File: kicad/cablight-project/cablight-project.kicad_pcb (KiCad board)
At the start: 4 copper layers, 70.1 x 40 mm, 55 parts, among them J3 Screw_Term_1x4_5mm, M2.5 MountingHole_2.7mm_M2.5_ISO73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, Q1 IRLB8721PBF, SW3 switch_SPDT_SLW_121586, T1 ISL85410, U3 ESP32-S3-WROOM-1U

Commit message: drc checks
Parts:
- moved R1 1.00 mm to (-52.5, 5.50)
- moved D2 0.40 mm to (-32.1, 2.50)
- moved M2.5 0.18 mm to (-24.6, 3.15)
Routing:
- net BTN: track 45.1 -> 46.7 mm
- net /VBUS: track 31.1 -> 30.5 mm
- net D-: track 14.4 -> 15.0 mm

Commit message: 99 percent layout v1
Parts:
- added M2.5: MountingHole_2.7mm_M2.5_ISO7380_Pad_TopOnly, MountingHole:MountingHole_2.7mm_M2.5_ISO7380_Pad_TopOnly, F.Cu at (-24.6, 29.4)
- C13: moved to B.Cu
- moved C13 8.41 mm to (-24.6, 25.9), turned to 180 degrees
- moved R2 5.47 mm to (-46.8, 28.6)
- moved BOOT1 5.04 mm to (-40.4, 25.4), turned to 180 degrees
- moved RESET1 4.72 mm to (-47.8, 25.4), turned to 180 degrees
- moved C6 3.26 mm to (-51.2, 22.6)
- moved R3 2.93 mm to (-51.1, 25.4)
- moved C7 1.37 mm to (-46.7, 26.1)
- moved RCWL-1601 0.60 mm to (-24.6, 17.1)
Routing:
- net 3.3V: track 61.7 -> 141.2 mm, vias 4 -> 6
- net Net-(D10-A): track 0.20 -> 5.41 mm
- net BTN: track 46.7 -> 44.3 mm
- net PG: track 44.6 -> 42.4 mm
- net Net-(T1-FB): track 7.24 -> 9.34 mm
- net GND: track 6.11 -> 7.49 mm, vias 12 -> 15
- net Net-(USBC-V1-CC2): track 7.35 -> 8.62 mm
- net Net-(U3-GPIO0/BOOT): track 42.4 -> 41.2 mm
- net 24VDC: track 15.0 -> 14.5 mm
- net ECHO: track 23.8 -> 24.4 mm
- net DIP3: track 24.4 -> 23.9 mm
- added copper zone on In2.Cu, net GND
- removed copper zone on In2.Cu, net 3.3V
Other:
- outline, holes or cut-outs redrawn
- board text added: "C11~"
- board text removed: "TURN THESE AROUND"

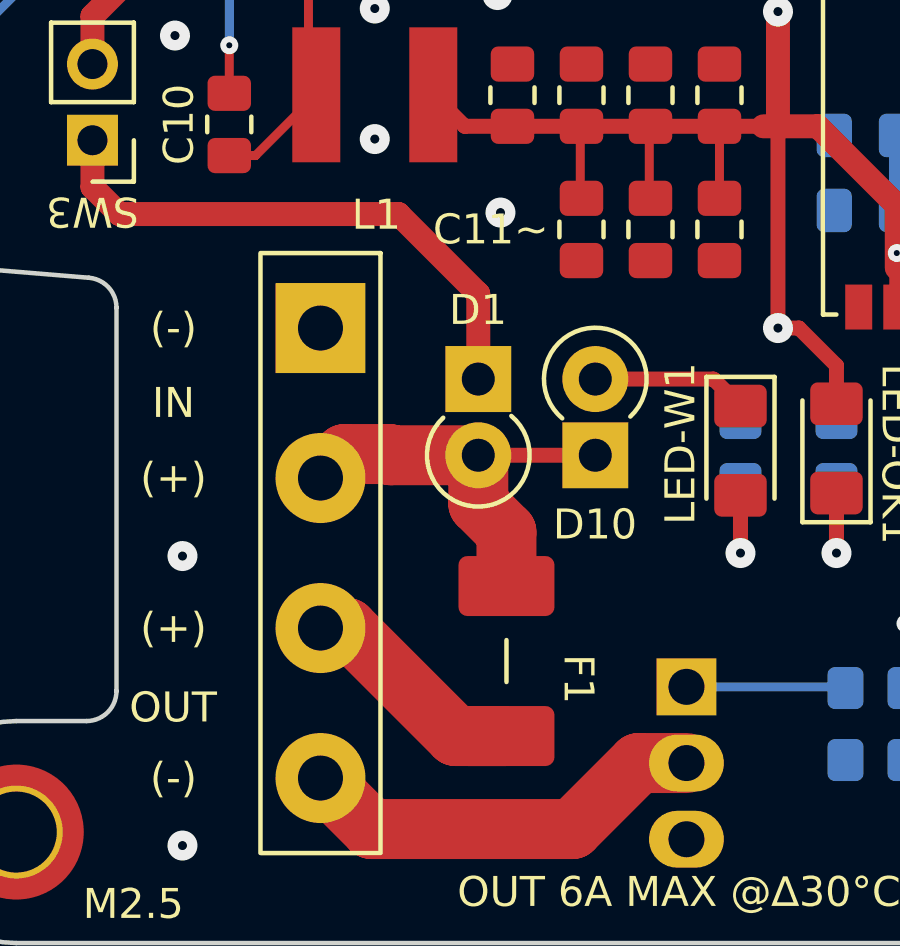
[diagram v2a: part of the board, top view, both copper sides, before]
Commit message: change fuse pkg & add datasheets
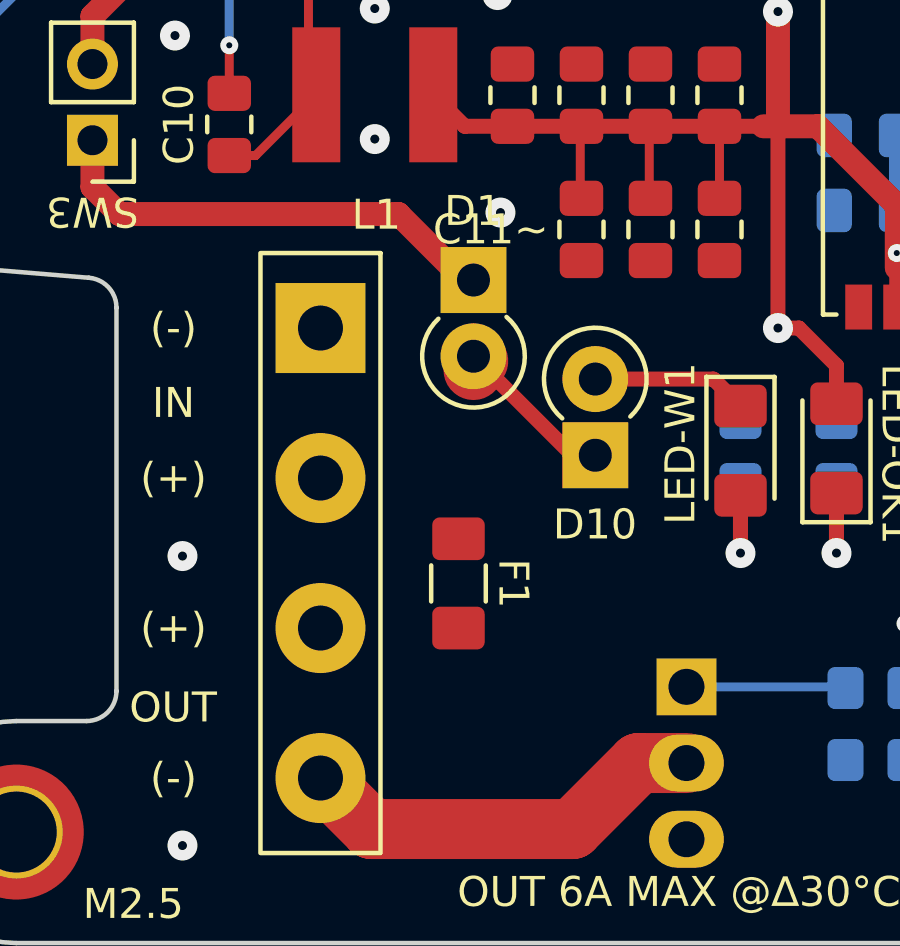
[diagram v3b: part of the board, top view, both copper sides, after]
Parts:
- F1: footprint GRK_Lib:Fuse SMD pkg 0679L -> Fuse:Fuse_1206_3216Metric_Pad1.42x1.75mm_HandSolder
- moved D1 3.30 mm to (-68.9, 17.9)
- moved F1 1.60 mm to (-69.4, 28.0)
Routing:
- net 24VDC: track 14.5 -> 6.11 mm
- net /LED+: track 7.69 -> 0.00 mm
- net Net-(D1-K): track 18.7 -> 15.5 mm
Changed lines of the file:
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@@
 			)
 		)
-		(property "Datasheet" "~"
+		(property "Datasheet" "kicad-embed://Wurth Semi-Sheilded Power Inductor 22uH SMT.pdf"
 			(at 0 0 0)
 			(unlocked yes)
@@
 			)
 		)
-		(property "Datasheet" ""
+		(property "Datasheet" "kicad-embed://ISL85410.pdf"
 			(at 0 0 90)
 			(unlocked yes)
@@
 			)
 		)
-		(property "Description" ""
+		(property "Description" "Buck Voltage Regulator"
 			(at 0 0 90)
 			(unlocked yes)
@@
 			)
 		)
-		(property "Datasheet" "https://www.espressif.com/sites/default/files/documentation/esp32-s3-wroom-1_wroom-1u_datasheet_en.pdf"
+		(property "Datasheet" "kicad-embed://esp32-s3-wroom-1_wroom-1u_datasheet_en.pdf"
 			(at 0 0 90)
 			(unlocked yes)
@@
 		(embedded_fonts no)
 	)
-	(footprint "GRK_Lib:Fuse SMD pkg 0679L"
+	(footprint "Fuse:Fuse_1206_3216Metric_Pad1.42x1.75mm_HandSolder"
 		(layer "F.Cu")
-		(at -67.8 28.1 -90)
+		(at -69.4 28.0125 -90)
+		(descr "Fuse SMD 1206 (3216 Metric), square (rectangular) end terminal, IPC-7351 nominal with elongated pad for handsoldering. (Body size source: http://www.tortai-tech.com/upload/download/2011102023233369053.pdf), generated with kicad-footprint-generator")
+		(tags "fuse handsolder")
 		(property "Reference" "F1"
-			(at 3.1 -2.4 270)
+			(at 0 -1.83 270)
 			(unlocked yes)
 			(layer "F.SilkS")
@@
 		)
 		(property "Value" "8A"
-			(at -0.05 9.5 270)
+			(at 0 1.83 270)
 			(unlocked yes)
 			(layer "F.Fab")
-			(hide yes)
 			(effects
 				(font
@@
 		(attr smd)
 		(fp_line
-			(start 1.8 0)
-			(end 3.2 0)
+			(start -0.602064 0.91)
+			(end 0.602064 0.91)
 			(stroke
 				(width 0.15)
@@
 			(layer "F.SilkS")
 		)
-		(fp_rect
-			(start -2 -3)
-			(end 7.1 3.1)
+		(fp_line
+			(start -0.602064 -0.91)
+			(end 0.602064 -0.91)
+			(stroke
+				(width 0.15)
+				(type solid)
+			)
+			(layer "F.SilkS")
+		)
+		(fp_line
+			(start -2.45 1.13)
+			(end -2.45 -1.13)
 			(stroke
 				(width 0.15)
 				(type solid)
 			)
-			(fill no)
 			(layer "F.CrtYd")
 		)
-		(pad "1" smd roundrect
+		(fp_line
+			(start 2.45 1.13)
+			(end -2.45 1.13)
+			(stroke
+				(width 0.15)
+				(type solid)
+			)
+			(layer "F.CrtYd")
+		)
+		(fp_line
+			(start -2.45 -1.13)
+			(end 2.45 -1.13)
+			(stroke
+				(width 0.15)
+				(type solid)
+			)
+			(layer "F.CrtYd")
+		)
+		(fp_line
+			(start 2.45 -1.13)
+			(end 2.45 1.13)
+			(stroke
+				(width 0.15)
+				(type solid)
+			)
+			(layer "F.CrtYd")
+		)
+		(fp_line
+			(start -1.6 0.8)
+			(end -1.6 -0.8)
+			(stroke
+				(width 0.15)
+				(type solid)
+			)
+			(layer "F.Fab")
+		)
+		(fp_line
+			(start 1.6 0.8)
+			(end -1.6 0.8)
+			(stroke
+				(width 0.15)
+				(type solid)
+			)
+			(layer "F.Fab")
+		)
+		(fp_line
+			(start -1.6 -0.8)
+			(end 1.6 -0.8)
+			(stroke
+				(width 0.15)
+				(type solid)
+			)
+			(layer "F.Fab")
+		)
+		(fp_line
+			(start 1.6 -0.8)
+			(end 1.6 0.8)
+			(stroke
+				(width 0.15)
+				(type solid)
+			)
+			(layer "F.Fab")
+		)
+		(fp_text user "${REFERENCE}"
 			(at 0 0 270)
-			(size 2 3.2)
+			(unlocked yes)
+			(layer "F.Fab")
+			(effects
+				(font
+					(size 1 1)
+					(thickness 0.15)
+				)
+			)
+		)
+		(pad "1" smd roundrect
+			(at -1.4875 0 270)
+			(size 1.425 1.75)
 			(layers "F.Cu" "F.Mask" "F.Paste")
-			(roundrect_rratio 0.15)
+			(roundrect_rratio 0.175439)
 			(net 20 "24VDC")
 			(pintype "passive")
 		)
 		(pad "2" smd roundrect
-			(at 5 0 270)
-			(size 2 3.2)
+			(at 1.4875 0 270)
+			(size 1.425 1.75)
 			(layers "F.Cu" "F.Mask" "F.Paste")
-			(roundrect_rratio 0.15)
+			(roundrect_rratio 0.175439)
 			(net 16 "/LED+")
 			(pintype "passive")
 		)
 		(embedded_fonts no)
+		(model "${KICAD9_3DMODEL_DIR}/Fuse.3dshapes/Fuse_1206_3216Metric.wrl"
+			(offset
+				(xyz 0 0 0)
+			)
+			(scale
+				(xyz 1 1 1)
+			)
+			(rotate
+				(xyz 0 0 0)
+			)
+		)
 	)
 	(footprint "Diode_THT:D_DO-41_SOD81_P2.54mm_Vertical_KathodeUp"
 		(layer "F.Cu")
-		(at -68.74 21.2 -90)
+		(at -68.9 17.9 -90)
 		(descr "Diode, DO-41_SOD81 series, Axial, Vertical, pin pitch=2.54mm, , length*diameter=5.2*2.7mm^2, , http://www.diodes.com/_files/packages/DO-41%20(Plastic).pdf")
 		(tags "Diode DO-41_SOD81 series Axial Vertical pin pitch 2.54mm  length 5.2mm diameter 2.7mm")
@@
 			)
 		)
-		(property "Datasheet" "~"
+		(property "Datasheet" "kicad-embed://1N5817-D.PDF"
 			(at 0 0 270)
 			(unlocked yes)
@@
 			)
 		)
-		(property "Datasheet" "~"
+		(property "Datasheet" "kicad-embed://shunt-jumper-254mm-msa-g-data-sheet.pdf"
 			(at 0 0 180)
 			(unlocked yes)
@@
 	)
 	(segment
-		(start -69.5 33.1)
-		(end -67.8 33.1)
-		(width 2)
-		(layer "F.Cu")
-		(net 16)
-	)
-	(segment
-		(start -73.1 29.5)
-		(end -69.5 33.1)
-		(width 2)
-		(layer "F.Cu")
-		(net 16)
-	)
-	(segment
-		(start -74 29.5)
-		(end -73.1 29.5)
-		(width 2)
-		(layer "F.Cu")
-		(net 16)
-	)
-	(segment
 		(start -31.1 28.2)
 		(end -32 27.3)
@@
 	)
 	(segment
-		(start -68.9 23.74)
-		(end -68.74 23.58)
-		(width 0.3)
-		(layer "F.Cu")
-		(net 20)
-	)
-	(segment
-		(start -68.74 23.74)
+		(start -65.6 23.74)
 		(end -64.84 23.74)
 		(width 0.5)
@@
 	)
 	(segment
-		(start -71.66 23.74)
-		(end -68.74 23.74)
-		(width 2)
-		(layer "F.Cu")
-		(net 20)
-	)
-	(segment
-		(start -67.8 26.3)
-		(end -68.74 25.36)
-		(width 2)
-		(layer "F.Cu")
-		(net 20)
-	)
-	(segment
-		(start -71.7 23.7)
-		(end -71.66 23.74)
-		(width 2)
-		(layer "F.Cu")
-		(net 20)
-	)
-	(segment
-		(start -67.8 28.1)
-		(end -67.8 26.3)
-		(width 2)
-		(layer "F.Cu")
-		(net 20)
-	)
-	(segment
-		(start -68.74 25.36)
-		(end -68.74 23.74)
+		(start -68.74 20.6)
+		(end -68.9 20.44)
 		(width 2)
 		(layer "F.Cu")
@@
 	)
 	(segment
-		(start -73.2 23.7)
-		(end -71.7 23.7)
+		(start -68.9 20.9)
+		(end -68.9 20.44)
 		(width 2)
 		(layer "F.Cu")
@@
 	)
 	(segment
-		(start -74 24.5)
-		(end -73.2 23.7)
-		(width 2)
+		(start -68.9 20.44)
+		(end -65.6 23.74)
+		(width 0.5)
 		(layer "F.Cu")
 		(net 20)
@@
 	)
 	(segment
-		(start -68.74 18.36)
-		(end -68.74 21.2)
+		(start -81.6 13.24)
+		(end -81.6 14.8)
 		(width 0.8)
 		(layer "F.Cu")
@@
 	)
 	(segment
-		(start -81.6 14.8)
-		(end -80.7 15.7)
+		(start -69.2 17.9)
+		(end -68.9 17.9)
 		(width 0.8)
 		(layer "F.Cu")
@@
 	)
 	(segment
-		(start -80.7 15.7)
-		(end -71.4 15.7)
+		(start -71.4 15.7)
+		(end -69.2 17.9)
 		(width 0.8)
 		(layer "F.Cu")
@@
 	)
 	(segment
-		(start -81.6 13.24)
-		(end -81.6 14.8)
+		(start -81.6 14.8)
+		(end -80.7 15.7)
 		(width 0.8)
 		(layer "F.Cu")
@@
 	)
 	(segment
-		(start -71.4 15.7)
-		(end -68.74 18.36)
+		(start -80.7 15.7)
+		(end -71.4 15.7)
 		(width 0.8)
 		(layer "F.Cu")
@@
 		(min_thickness 0.25)
 		(filled_areas_thickness no)
-		(fill yes
+		(fill
 			(thermal_gap 0.3)
 			(thermal_bridge_width 0.3)

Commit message: progress
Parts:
- added R15: 0, Resistor_SMD:R_0805_2012Metric_Pad1.20x1.40mm_HandSolder, B.Cu at (-60.0, 19.1)
- added R17: 0, Resistor_SMD:R_0805_2012Metric_Pad1.20x1.40mm_HandSolder, B.Cu at (-56.9, 19.1)
- C6, C7: value 1uF -> 0u1F
- moved C3 7.07 mm to (-49.3, 15.8), turned to 90 degrees
- moved C4 6.31 mm to (-52.5, 9.60)
- moved C5 4.04 mm to (-51.8, 15.8), turned to 90 degrees
- moved D1 3.31 mm to (-68.6, 21.2)
- moved F1 2.13 mm to (-67.7, 29.3)
- moved Q1 1.30 mm to (-63.1, 31.5)
- moved J3 0.92 mm to (-73.4, 20.2)
- moved SW3 0.48 mm to (-81.4, 12.8)
- moved C10 0.06 mm to (-77.0, 12.7)
- renumbered C13 to C14, C11A1 to CP1, C11B1 to CP2, C11C1 to CP3, C11D1 to CP4, C11E1 to CP5, C11F1 to CP6, C11G1 to CP7
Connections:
- R14 pad 2: GND -> Net-(R14-Pad2)
- R16 pad 2: GND -> Net-(R15-Pad1)
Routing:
- net PG: track 42.4 -> 30.1 mm
- net /LED-: track 13.8 -> 21.6 mm
- net 24VDC: track 6.11 -> 0.76 mm, vias 0 -> 7
- net GND: track 7.49 -> 2.76 mm, vias 15 -> 20
- net 3.3V: track 141.2 -> 145.9 mm
- net Net-(D1-K): track 15.5 -> 19.3 mm
- net Net-(R14-Pad2): track 0.00 -> 2.52 mm
- net Net-(R15-Pad1): track 0.00 -> 2.52 mm
- net Net-(Q1-G): track 5.32 -> 6.62 mm
- net BTN: track 44.3 -> 43.5 mm
- net Net-(T1-PHASE): track 11.0 -> 10.2 mm
- net 5V: track 59.4 -> 58.8 mm
- net /LED+: vias 0 -> 4
- added copper zone on B.Cu, net /LED+
- added copper zone on F.Cu, net /LED+
- added copper zone on B.Cu, net 24VDC
- added copper zone on F.Cu, net 24VDC

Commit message: changes
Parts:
- added REF**: MountingHole_3.2mm_M3_DIN965_Pad_TopBottom, MountingHole:MountingHole_3.2mm_M3_DIN965_Pad_TopBottom, F.Cu at (-45.8, 34.0)
- added TP1: 3V3, TestPoint:TestPoint_THTPad_D1.0mm_Drill0.5mm, F.Cu at (-60.6, 5.00)
- added TP2: GND, TestPoint:TestPoint_THTPad_D1.0mm_Drill0.5mm, F.Cu at (-35.2, 5.30)
- C14, C3, C5: moved to F.Cu
- LED-OK1, LED-W1: footprint LED_SMD:LED_1206_3216Metric_Pad1.42x1.75mm_HandSolder -> LED_SMD:LED_0603_1608Metric_Pad1.05x0.95mm_HandSolder
- moved C3 10.9 mm to (-55.4, 24.7), turned to -90 degrees
- moved C5 10.7 mm to (-57.6, 24.7), turned to -90 degrees
- moved C14 8.32 mm to (-27.7, 18.1), turned to -90 degrees
- moved C4 5.88 mm to (-54.5, 15.1), turned to 180 degrees
- moved LED-OK1 5.17 mm to (-60.7, 26.9)
- moved R14 5.17 mm to (-60.7, 27.0)
- moved R17 5.17 mm to (-60.8, 22.5)
- moved R16 2.28 mm to (-60.7, 21.4)
- moved R15 2.28 mm to (-60.7, 17.0)
- moved LED-W1 1.53 mm to (-60.7, 22.2)
- moved R1 1.35 mm to (-52.5, 4.15)
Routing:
- net 3.3V: track 145.9 -> 132.3 mm, vias 6 -> 4
- net LEDSIG: track 44.3 -> 56.3 mm, vias 2 -> 1
- net PG: track 30.1 -> 40.0 mm, vias 3 -> 4
- net Net-(D10-A): track 5.41 -> 0.00 mm
- net Net-(LED-OK1-K): track 4.40 -> 0.00 mm
- net Net-(LED-W1-A): track 4.32 -> 0.00 mm
- net Net-(U3-GPIO0/BOOT): track 41.2 -> 38.5 mm
- net BTN: track 43.5 -> 41.4 mm
- net 5V: track 58.8 -> 60.2 mm
- net GND: vias 20 -> 40
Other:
- board text added: "+-!"
- board text added: "MAX OUT 5A @∆20°C"
- board text added: "PWR"
- board text removed: "OUT 6A MAX @∆30°C"

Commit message: plot fab for final check
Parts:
- added U1: TPD2EUSB30, GRK_Lib:DRT3, F.Cu at (108.4, 65.0)
- moved R15 157.3 mm to (89.2, 64.5), turned to 180 degrees
- moved R17 157.0 mm to (89.2, 69.1), turned to 180 degrees
- moved R16 156.6 mm to (89.2, 66.8), turned to 0 degrees
- moved R14 156.4 mm to (89.2, 71.5), turned to 0 degrees
- moved C7 154.6 mm to (101.6, 69.8)
- moved R2 154.6 mm to (101.6, 72.3)
- moved RCWL-1601 154.5 mm to (123.7, 60.7)
- moved M2.5 154.4 mm to (64.0, 80.0)
- moved R13 154.3 mm to (117.4, 69.5)
- moved M2.5 154.2 mm to (123.2, 47.0)
- moved M2.5 154.2 mm to (123.2, 73.3)
- moved S1 154.0 mm to (129.1, 59.8)
- moved C14 153.9 mm to (119.9, 61.8)
- moved BOOT1 153.8 mm to (107.0, 69.5)
- moved C6 153.8 mm to (96.2, 66.7)
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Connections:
- net Net-(T1-PHASE) renamed /PSU_PHASE
- DIP1 pad 1: GND -> LEDSIG
- DIP1 pad 4: LEDSIG -> GND
- DIP1 pad 5: DIP4 -> DIP3
- DIP1 pad 6: DIP3 -> DIP2
- DIP1 pad 7: DIP2 -> DIP1
- DIP1 pad 8: DIP1 -> 3.3V
- U3 pad 12: unconnected-(U3-GPIO8/TOUCH8/ADC1_CH7/SUBSPICS1-Pad12) -> DIP3
- U3 pad 17: DIP4 -> unconnected-(U3-GPIO9/TOUCH9/ADC1_CH8/FSPIHD/SUBSPIHD-Pad17)
- U3 pad 18: DIP3 -> unconnected-(U3-GPIO10/TOUCH10/ADC1_CH9/FSPICS0/FSPIIO4/SUBSPICS0-Pad18)
- U3 pad 5: LEDSIG -> unconnected-(U3-GPIO5/TOUCH5/ADC1_CH4-Pad5)
- U3 pad 7: unconnected-(U3-GPIO7/TOUCH7/ADC1_CH6-Pad7) -> LEDSIG
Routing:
- net 3.3V: track 132.3 -> 86.9 mm
- net /LED-: track 21.6 -> 0.00 mm
- net DIP4: track 19.2 -> 0.00 mm, vias 1 -> 0
- net LEDSIG: track 56.3 -> 39.9 mm
- net /VBUS: track 30.5 -> 24.3 mm
- net DIP1: track 21.2 -> 15.2 mm
- net Net-(LED-W1-A): track 0.00 -> 5.53 mm
- net /PSU_PHASE: track 10.2 -> 4.84 mm
- net Net-(LED-OK1-K): track 0.00 -> 5.34 mm
- net DIP3: track 23.6 -> 18.8 mm
- net Net-(D10-A): track 0.00 -> 4.29 mm
- net D+: track 13.4 -> 16.4 mm
- net D-: track 15.0 -> 17.6 mm
- net TRIG: track 23.5 -> 25.4 mm
- net PG: track 40.0 -> 41.8 mm, vias 4 -> 3
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- added copper zone on B.Cu, net /LED-
- added copper zone on F.Cu, net /LED-
- added copper zone on F.Cu, net /PSU_PHASE
- added copper zone on F.Cu, net /VBUS
- added copper zone on F.Cu, net 3.3V
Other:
- board size 70.1 x 40 mm -> 71.4 x 40 mm
- board text added: "RATED 5-24V DC 5A"
- board text removed: "MAX OUT 5A @∆20°C"
